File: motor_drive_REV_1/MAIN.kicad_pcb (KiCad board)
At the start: 2 copper layers, 71 parts, among them J1 Conn_01x02, J2 Conn_01x03, J3 Conn_01x06, J4 Conn_01x06, Q1 nmos, Q2 nmos, Q3 nmos, Q4 nmos, Q5 nmos, Q6 nmos, U1 AD8418ABRMZ-RL, U2 AD8418ABRMZ-RL, U3 AD8418ABRMZ-RL, U4 AD8418ABRMZ-RL, U5 ADA4571WHRZ-R7, U6 SN65LBC176QDRQ1, U7 FAN7888_gen, U8 TMS320F28027PTT, U9 AD8418ABRMZ-RL

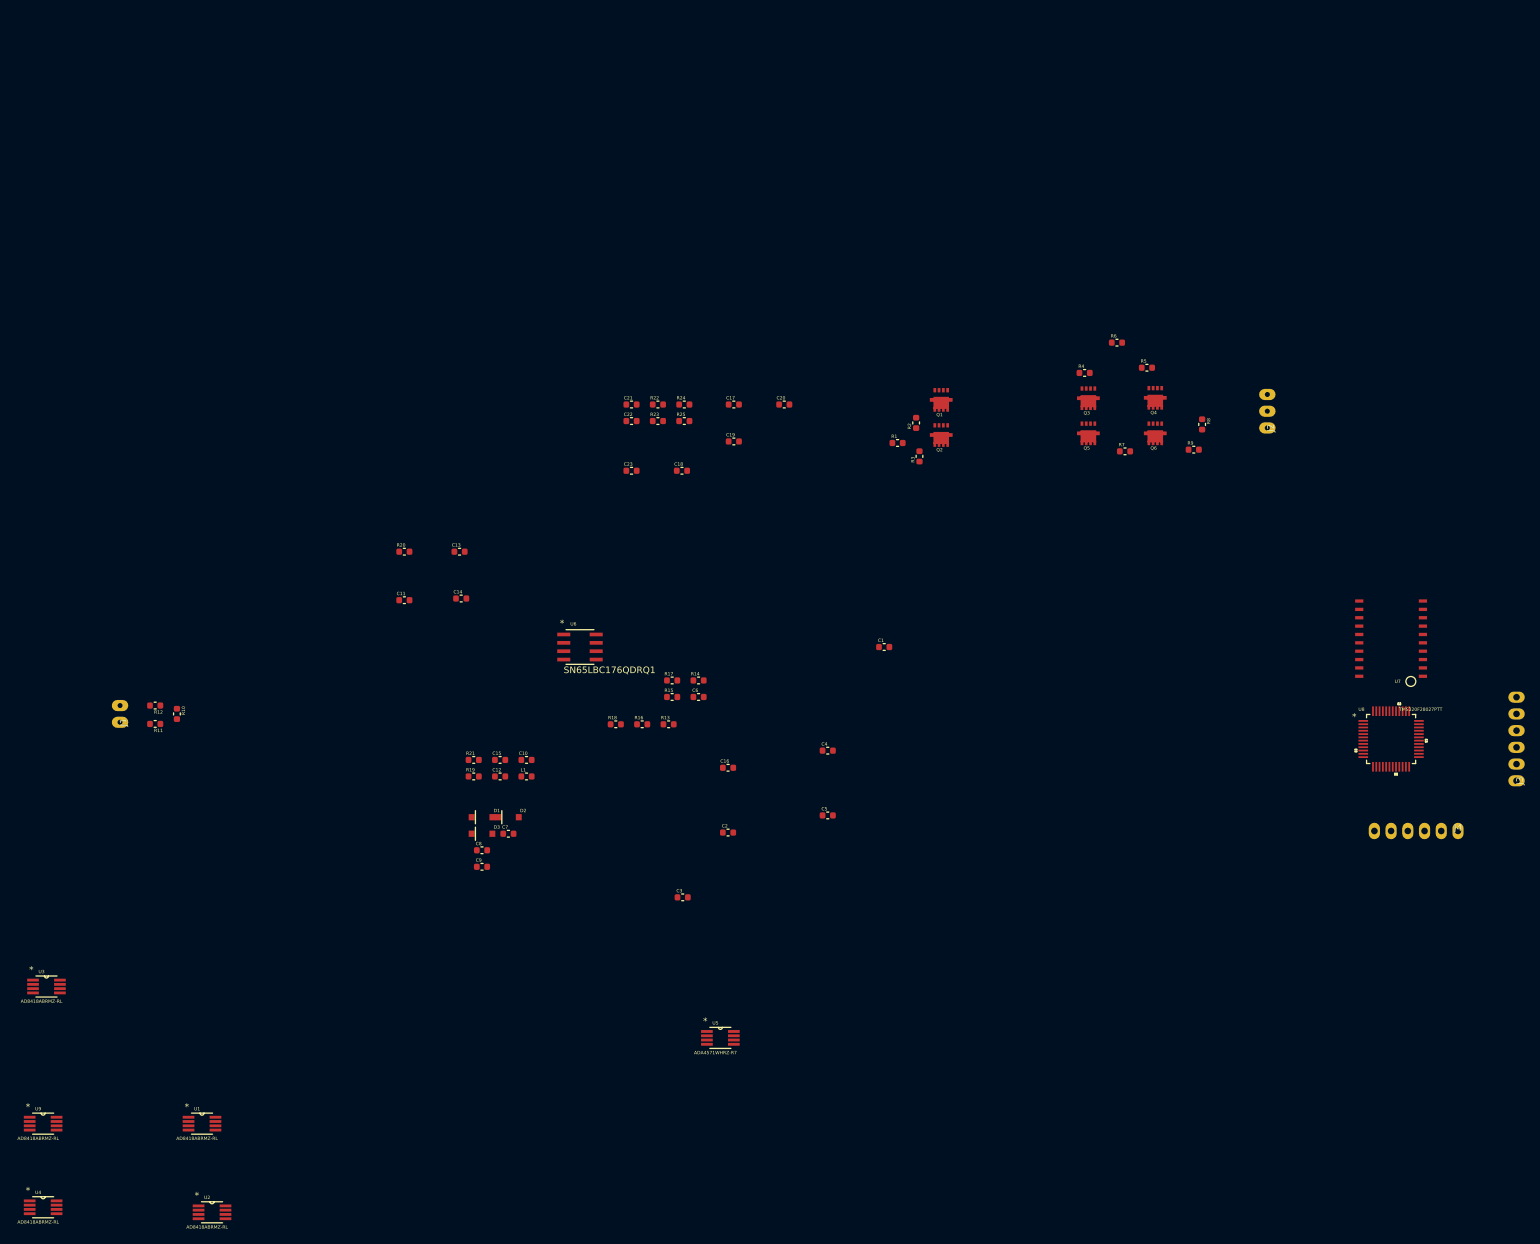
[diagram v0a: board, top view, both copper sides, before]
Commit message: working on adding thermistors but encountered too many hierarchicaly copies bug
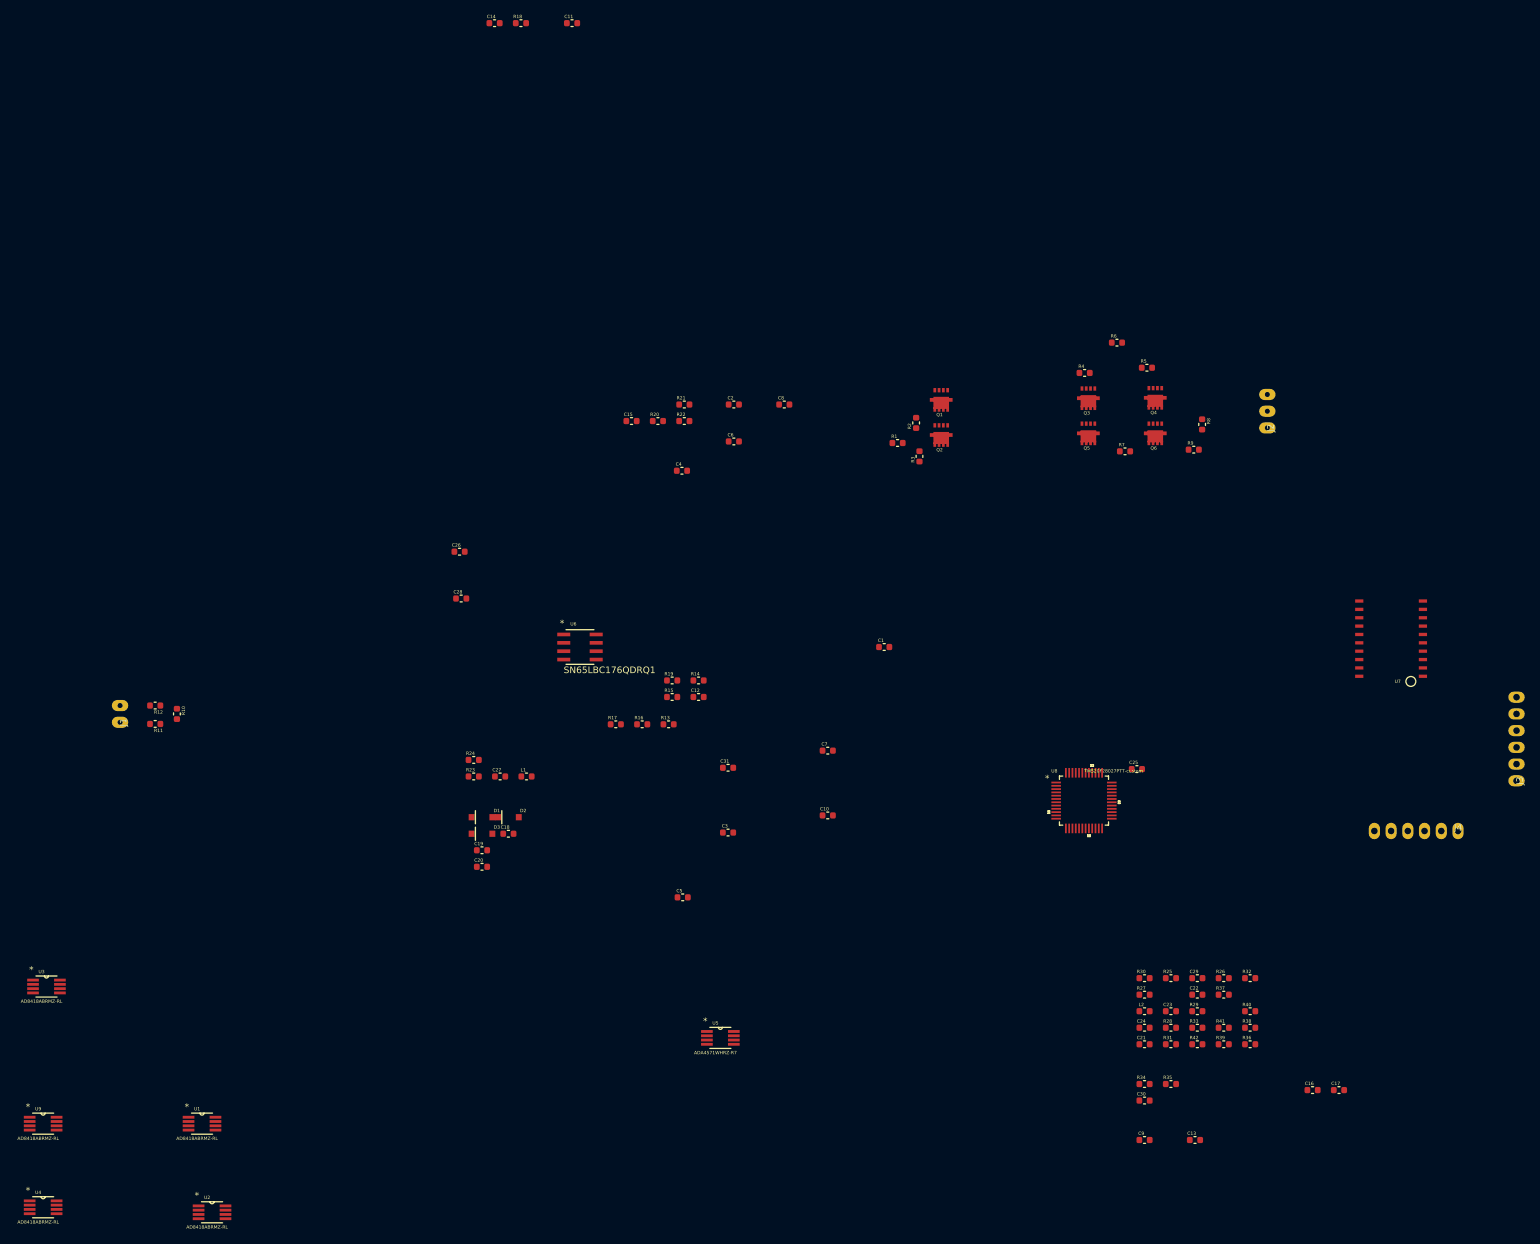
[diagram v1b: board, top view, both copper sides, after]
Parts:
- removed the C10 at (125.2, 97.2)
- removed the C15 at (121.2, 97.2)
- removed the R20 at (106.7, 65.5)
- removed the R22 at (145.2, 43.2)
- added C13: 0.01uF, motor_drive_footprints:C_0603_1608Metric, F.Cu at (226.8, 154.9)
- added C14: 680pF, motor_drive_footprints:C_0603_1608Metric, F.Cu at (120.4, -14.7)
- added C16: 2.2uF, motor_drive_footprints:C_0603_1608Metric, F.Cu at (244.6, 147.3)
- added C17: 0.01uF, motor_drive_footprints:C_0603_1608Metric, F.Cu at (248.6, 147.3)
- added C22: 2.2uF, motor_drive_footprints:C_0603_1608Metric, F.Cu at (227.1, 132.8)
- added C24: 0.01uF, motor_drive_footprints:C_0603_1608Metric, F.Cu at (219.1, 137.8)
- added C25: 4.7uF, motor_drive_footprints:C_0603_1608Metric, F.Cu at (217.9, 98.6)
- added C29: 1uF, motor_drive_footprints:C_0603_1608Metric, F.Cu at (227.1, 130.3)
- added C30: 1uF, motor_drive_footprints:C_0603_1608Metric, F.Cu at (219.1, 148.9)
- added C9: 0.01uF, motor_drive_footprints:C_0603_1608Metric, F.Cu at (219.1, 154.9)
- added L2: 2.2uF, motor_drive_footprints:C_0603_1608Metric, F.Cu at (219.1, 135.3)
- added R18: 680, motor_drive_footprints:C_0603_1608Metric, F.Cu at (124.4, -14.7)
- added R25: 375, motor_drive_footprints:C_0603_1608Metric, F.Cu at (223.1, 130.3)
- added R26: 2.2k, motor_drive_footprints:C_0603_1608Metric, F.Cu at (231.1, 130.3)
- added R27: 10k, motor_drive_footprints:C_0603_1608Metric, F.Cu at (219.1, 132.8)
- added R28: 10k, motor_drive_footprints:C_0603_1608Metric, F.Cu at (223.1, 137.8)
- added R29: 10k, motor_drive_footprints:C_0603_1608Metric, F.Cu at (227.1, 135.3)
- added R30: 10k, motor_drive_footprints:C_0603_1608Metric, F.Cu at (219.1, 130.3)
- added R31: 10k, motor_drive_footprints:C_0603_1608Metric, F.Cu at (223.1, 140.3)
- added R32: 10k, motor_drive_footprints:C_0603_1608Metric, F.Cu at (235.1, 130.3)
- added R33: 10k, motor_drive_footprints:C_0603_1608Metric, F.Cu at (227.1, 137.8)
- added R34: 10k, motor_drive_footprints:C_0603_1608Metric, F.Cu at (219.1, 146.4)
- added R35: 375, motor_drive_footprints:C_0603_1608Metric, F.Cu at (223.1, 146.4)
- added R36: 375, motor_drive_footprints:C_0603_1608Metric, F.Cu at (235.1, 140.3)
- added R37: 375, motor_drive_footprints:C_0603_1608Metric, F.Cu at (231.1, 132.8)
- added R38: 375, motor_drive_footprints:C_0603_1608Metric, F.Cu at (235.1, 137.8)
- added R39: 375, motor_drive_footprints:C_0603_1608Metric, F.Cu at (231.1, 140.3)
- added R40: 375, motor_drive_footprints:C_0603_1608Metric, F.Cu at (235.1, 135.3)
- added R41: 375, motor_drive_footprints:C_0603_1608Metric, F.Cu at (231.1, 137.8)
- added R42: 375, motor_drive_footprints:C_0603_1608Metric, F.Cu at (227.1, 140.3)
- C10: renamed from C5; value C -> 2.2uF
- C11: value C -> 0.01uF
- C12: renamed from C6; value C -> 2.2uF
- C15: renamed from C22; value C -> 680pF
- C18: renamed from C7; value C -> 0.22uF
- C19: renamed from C8; value C -> 0.22uF
- C20: renamed from C9; value C -> 0.22uF
- C21: value C -> 2.2uF
- C26: renamed from C13; value C -> 1uF
- C27: renamed from C12; value C -> 100pF
- C28: renamed from C14; value C -> 4.7uF
- C31: renamed from C16; value 1uF -> 0.01uF
- L1: value L -> 2.2uF
- R1, R2, R4, R5, R7, R8: value R -> 10
- R24: renamed from R21; value R -> 4.7k
- R3, R6, R9: value R -> 0.005
- U8: value TMS320F28027PTT -> TMS20F28027PTT-custom
- moved C21 124.5 mm to (219.1, 140.3)
- moved C23 116.0 mm to (223.1, 135.3)
- moved C11 91.3 mm to (132.1, -14.7)
- moved U8 47.6 mm to (209.9, 103.3)
- renumbered C17 to C2, C2 to C3, C18 to C4, C3 to C5, C19 to C6, C4 to C7, C20 to C8, R18 to R17, R17 to R19, R23 to R20, R24 to R21, R25 to R22, R19 to R23
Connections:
- C1 pad 1: /5.0V -> /GND
- C10 pad 2: /5.0V -> /GND
- C11 pad 1: /5.0V -> Net-(C11-Pad1)
- C11 pad 2: /5.0V -> Net-(C11-Pad2)
- C12 pad 2: /5.0V -> /GND
- C15 pad 1: /5.0V -> /GND
- C15 pad 2: /5.0V -> Net-(C15-Pad2)
- C2 pad 1: /5.0V -> /GND
- C21 pad 2: /5.0V -> /GND
- C23 pad 2: /5.0V -> /GND
- C26 pad 1: /5.0V -> Net-(C26-Pad1)
- C26 pad 2: /5.0V -> /GND
- C27 pad 1: /5.0V -> /GND
- C27 pad 2: Net-(C12-Pad2) -> /chip_reset
- C28 pad 1: Net-(C14-Pad1) -> Net-(C28-Pad1)
- C28 pad 2: /5.0V -> /GND
- C3 pad 1: /5.0V -> /GND
- C31 pad 1: /5.0V -> /GND
- C4 pad 1: /5.0V -> /GND
- C5 pad 1: /5.0V -> /GND
- C6 pad 1: /5.0V -> /GND
- C7 pad 1: /5.0V -> /GND
- C8 pad 1: /5.0V -> /GND
- J3 pad 3: /CLK -> /nEN
- J3 pad 4: /nEN -> /CLK
- J3 pad 6: /5.0V -> /GND
- J4 pad 6: /5.0V -> /GND
- L1 pad 1: Net-(C14-Pad1) -> Net-(C26-Pad1)
- R14 pad 2: /5.0V -> /GND
- R17 pad 1: /5.0V -> /GND
- R17 pad 2: /5.0V -> /balance
- R19 pad 1: /5.0V -> Net-(C14-Pad1)
- R19 pad 2: /5.0V -> Net-(C15-Pad2)
- R20 pad 1: /5.0V -> /GND
- R20 pad 2: /5.0V -> Net-(C15-Pad2)
- R21 pad 1: /5.0V -> Net-(C14-Pad1)
- R22 pad 1: /5.0V -> Net-(C15-Pad2)
- R23 pad 1: Net-(C12-Pad2) -> /GND
- R23 pad 2: /5.0V -> Net-(R23-Pad2)
- R24 pad 1: /5.0V -> /GND
- U1 pad 2: /5.0V -> /GND
- U1 pad 3: /5.0V -> /GND
- U2 pad 2: /5.0V -> /GND
- U2 pad 3: /5.0V -> /GND
- U3 pad 2: /5.0V -> /GND
- U3 pad 3: /5.0V -> /GND
- U4 pad 2: /5.0V -> /GND
- U4 pad 3: /5.0V -> /GND
- U5 pad 1: /5.0V -> /GND
- U5 pad 3: /5.0V -> /GND
- U5 pad 6: /5.0V -> /GND
- U5 pad 8: /5.0V -> /GND
- U6 pad 5: /5.0V -> /GND
- U6 pad 6: /5.0V -> Net-(C15-Pad2)
- U6 pad 7: /5.0V -> Net-(C14-Pad1)
- U7 pad 11: /5.0V -> /GND
- U8 pad 10: /I_sense_1 -> /cos
- U8 pad 11: Net-(C14-Pad1) -> Net-(C28-Pad1)
- U8 pad 12: /5.0V -> /GND
- U8 pad 15: /IDC_sense -> /therm_1
- U8 pad 16: /VDC_sense -> /therm_2
- U8 pad 2: /F28027/JTAG_nTRST -> Net-(R23-Pad2)
- U8 pad 20: /F28027/JTAG_TDI -> Net-(R28-Pad1)
- U8 pad 21: /F28027/JTAG_TMS -> Net-(R30-Pad1)
- U8 pad 22: /F28027/JTAG_TDO -> Net-(R32-Pad1)
- U8 pad 23: /F28027/JTAG_TCK -> Net-(R34-Pad1)
- U8 pad 24: /CLK -> Net-(R27-Pad1)
- U8 pad 25: /nEN -> Net-(R29-Pad1)
- U8 pad 26: /MISO -> Net-(R31-Pad1)
- U8 pad 27: /MOSI -> Net-(R33-Pad1)
- U8 pad 28: /LS_1 -> /HS_1
- U8 pad 29: /HS_1 -> /LS_1
- U8 pad 3: Net-(C12-Pad2) -> /chip_reset
- U8 pad 33: /5.0V -> /GND
- U8 pad 35: /5.0V -> Net-(C26-Pad1)
- U8 pad 4: /sin -> /I_sense_1
- U8 pad 43: /5.0V -> /GND
- U8 pad 45: /5.0V -> Net-(U8-Pad45)
- U8 pad 5: /VDC_sense -> /I_sense_2
- U8 pad 6: /cos -> /I_sense_3
- U8 pad 8: /I_sense_2 -> /VDC_sense
- U8 pad 9: /I_sense_3 -> /sin
- U9 pad 2: /5.0V -> /GND
- U9 pad 3: /5.0V -> /GND

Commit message: started layout
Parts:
- removed the J2 at (237.7, 46.7)
- added C11: 1uF, motor_drive_footprints:gen_0805, F.Cu at (232.2, 150.9)
- added C12: 1uF, motor_drive_footprints:gen_0805, F.Cu at (227.9, 150.9)
- added C34: 0.01uF, motor_drive_footprints:C_0603_1608Metric, F.Cu at (158.0, 111.0)
- added C35: 0.01uF, motor_drive_footprints:C_0603_1608Metric, F.Cu at (147.3, 103.4)
- added C36: 4.7uF, motor_drive_footprints:C_0603_1608Metric, F.Cu at (158.0, 107.4)
- added C37: 1uF, motor_drive_footprints:C_0603_1608Metric, F.Cu at (158.0, 109.2)
- added C38: 100pF, motor_drive_footprints:C_0603_1608Metric, F.Cu at (140.4, 109.0)
- added C39: 4.7uF, motor_drive_footprints:C_0603_1608Metric, F.Cu at (140.5, 112.5)
- added C40: 1uF, motor_drive_footprints:C_0603_1608Metric, F.Cu at (140.5, 116.1)
- added C41: 1uF, motor_drive_footprints:C_0603_1608Metric, F.Cu at (74.8, 113.3)
- added C42: 0.01uF, motor_drive_footprints:C_0603_1608Metric, F.Cu at (78.8, 113.3)
- added C43: C, motor_drive_footprints:C_0603_1608Metric, F.Cu at (140.2, 95.2)
- added C44: C, motor_drive_footprints:C_0603_1608Metric, F.Cu at (147.8, 97.3)
- added J1: Conn_01x04, motor_drive_footprints:4pos_254, F.Cu at (122.9, 89.9)
- added J3: Conn_01x04, motor_drive_footprints:4pos_338, F.Cu at (249.4, 109.5)
- added J6: Conn_01x02, motor_drive_footprints:2pos_254, F.Cu at (139.5, 92.2)
- added J7: Conn_01x02, motor_drive_footprints:2pos_254, F.Cu at (147.2, 92.2)
- added R43: R, motor_drive_footprints:C_0603_1608Metric, F.Cu at (140.2, 97.3)
- added R44: R, motor_drive_footprints:C_0603_1608Metric, F.Cu at (147.8, 95.2)
- C10: value 2.2uF -> 1uF; footprint motor_drive_footprints:C_0603_1608Metric -> motor_drive_footprints:gen_0805
- C13: renamed from C11; value 0.01uF -> 1uF; footprint motor_drive_footprints:C_0603_1608Metric -> motor_drive_footprints:gen_0805
- C14: renamed from C12; value 2.2uF -> 1uF; footprint motor_drive_footprints:C_0603_1608Metric -> motor_drive_footprints:gen_0805
- C15: renamed from C13; value 0.01uF -> 1uF; footprint motor_drive_footprints:C_0603_1608Metric -> motor_drive_footprints:gen_0805
- C16: renamed from C14; value 680pF -> 1uF; footprint motor_drive_footprints:C_0603_1608Metric -> motor_drive_footprints:gen_0805
- C17: renamed from C15; value 680pF -> 1uF; footprint motor_drive_footprints:C_0603_1608Metric -> motor_drive_footprints:gen_0805
- C18: renamed from C16; value 2.2uF -> 1uF; footprint motor_drive_footprints:C_0603_1608Metric -> motor_drive_footprints:gen_0805
- C19: renamed from C17; value 0.01uF -> 1uF; footprint motor_drive_footprints:C_0603_1608Metric -> motor_drive_footprints:gen_0805
- C20: renamed from C18; value 0.22uF -> 1uF; footprint motor_drive_footprints:C_0603_1608Metric -> motor_drive_footprints:gen_0805
- C21: renamed from C19; value 0.22uF -> 2.2uF
- C22: renamed from C20; value 0.22uF -> 0.01uF
- C24: renamed from C22; value 2.2uF -> 0.01uF
- C25: renamed from C23; value 0.01uF -> 680pF
- C26: renamed from C24; value 0.01uF -> 680pF
- C27: renamed from C25; value 4.7uF -> 2.2uF
- C28: renamed from C26; value 1uF -> 0.01uF
- C29: renamed from C27; value 100pF -> 0.22uF
- C30: renamed from C28; value 4.7uF -> 0.22uF
- C31: renamed from C29; value 1uF -> 0.22uF
- C32: renamed from C30; value 1uF -> 2.2uF
- C33: renamed from C31; value 0.01uF -> 2.2uF
- C9: value 0.01uF -> 1uF; footprint motor_drive_footprints:C_0603_1608Metric -> motor_drive_footprints:gen_0805
- R3, R6, R9: value 0.005 -> WSL20101L000FEA18; footprint motor_drive_footprints:C_0603_1608Metric -> motor_drive_footprints:WSL20101L000FEA18
- moved C19 197.5 mm to (66.8, 70.3)
- moved C18 192.3 mm to (66.8, 74.2)
- moved C15 182.7 mm to (66.8, 66.5)
- moved C9 178.0 mm to (66.8, 62.7)
- moved C8 141.7 mm to (75.7, 153.7)
- moved C24 125.9 mm to (111.5, 83.1), turned to 180 degrees
- moved C6 125.6 mm to (75.7, 144.8)
- moved C23 122.6 mm to (111.5, 81.5), turned to 180 degrees
- moved C25 118.3 mm to (117.9, 81.3)
- moved J5 114.5 mm to (153.7, 126.5)
- moved C26 113.1 mm to (117.9, 87.4), turned to 180 degrees
- moved C2 112.7 mm to (74.9, 120.7)
- moved C1 111.3 mm to (74.9, 118.1)
- moved C30 111.1 mm to (213.4, 124.9), turned to 270 degrees
- moved C7 109.5 mm to (75.7, 149.6)
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- renumbered C21 to C23, J1 to J2, J3 to J4, J4 to J5, R12 to R10, R10 to R11, R11 to R12
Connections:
- C10 pad 1: /5.0V -> /DC_Link_Input/5.0V
- C10 pad 2: /GND -> /DC_Link_Input/GND
- C13 pad 1: Net-(C11-Pad1) -> /DC_Link_Input/5.0V
- C13 pad 2: Net-(C11-Pad2) -> /DC_Link_Input/GND
- C14 pad 1: /5.0V -> /DC_Link_Input/5.0V
- C14 pad 2: /GND -> /DC_Link_Input/GND
- C15 pad 1: /5.0V -> /DC_Link_Input/5.0V
- C15 pad 2: /GND -> /DC_Link_Input/GND
- C16 pad 1: Net-(C14-Pad1) -> /DC_Link_Input/5.0V
- C16 pad 2: /5.0V -> /DC_Link_Input/GND
- C17 pad 1: /GND -> /DC_Link_Input/5.0V
- C17 pad 2: Net-(C15-Pad2) -> /DC_Link_Input/GND
- C18 pad 1: /5.0V -> /DC_Link_Input/5.0V
- C18 pad 2: /GND -> /DC_Link_Input/GND
- C19 pad 1: /5.0V -> /DC_Link_Input/5.0V
- C19 pad 2: /GND -> /DC_Link_Input/GND
- C20 pad 1: Net-(C18-Pad1) -> /DC_Link_Input/5.0V
- C20 pad 2: /I_sense_p1 -> /DC_Link_Input/GND
- C21 pad 1: Net-(C19-Pad1) -> /5.0V
- C21 pad 2: /I_sense_p2 -> /GND
- C22 pad 1: Net-(C20-Pad1) -> (no net)
- C22 pad 2: /I_sense_p3 -> (no net)
- C25 pad 1: /5.0V -> Net-(C25-Pad1)
- C25 pad 2: /GND -> /5.0V
- C26 pad 1: /5.0V -> /GND
- C26 pad 2: /GND -> Net-(C26-Pad2)
- C28 pad 1: Net-(C26-Pad1) -> /5.0V
- C29 pad 1: /GND -> Net-(C29-Pad1)
- C29 pad 2: /chip_reset -> /I_sense_p1
- C30 pad 1: Net-(C28-Pad1) -> Net-(C30-Pad1)
- C30 pad 2: /GND -> /I_sense_p2
- C31 pad 1: /5.0V -> Net-(C31-Pad1)
- C31 pad 2: /GND -> /I_sense_p3
- C32 pad 1: /GND -> /5.0V
- C32 pad 2: /5.0V -> /GND
- C33 pad 1: /GND -> /5.0V
- C33 pad 2: /5.0V -> /GND
- D1 pad 1: Net-(C18-Pad1) -> Net-(C29-Pad1)
- D2 pad 1: Net-(C19-Pad1) -> Net-(C30-Pad1)
- D3 pad 1: Net-(C20-Pad1) -> Net-(C31-Pad1)
- J2 pad 2: /IDC_sense_n -> /IDC_sense_p
- L1 pad 1: Net-(C26-Pad1) -> Net-(C37-Pad1)
- L2 pad 2: Net-(C28-Pad1) -> Net-(C39-Pad1)
- R10 pad 2: /IDC_sense_n -> /IDC_sense_p
- R18 pad 1: Net-(C14-Pad1) -> Net-(C25-Pad1)
- R19 pad 1: Net-(C14-Pad1) -> Net-(C25-Pad1)
- R19 pad 2: Net-(C15-Pad2) -> Net-(C26-Pad2)
- R20 pad 2: Net-(C15-Pad2) -> Net-(C26-Pad2)
- R21 pad 1: Net-(C14-Pad1) -> Net-(C25-Pad1)
- R22 pad 1: Net-(C15-Pad2) -> Net-(C26-Pad2)
- U1 pad 1: /I_sense_2n -> (no net)
- U1 pad 4: Net-(U1-Pad4) -> (no net)
- U1 pad 8: /I_sense_2p -> (no net)
- U2 pad 1: /I_sense_3n -> (no net)
- U2 pad 4: Net-(U2-Pad4) -> (no net)
- U2 pad 8: /I_sense_3p -> (no net)
- U3 pad 1: /IDC_sense_n -> /DC_pos
- U3 pad 4: Net-(U3-Pad4) -> (no net)
- U3 pad 8: /DC_pos -> /IDC_sense_p
- U4 pad 4: Net-(U4-Pad4) -> (no net)
- U5 pad 5: Net-(U5-Pad5) -> (no net)
- U6 pad 6: Net-(C15-Pad2) -> Net-(C26-Pad2)
- U6 pad 7: Net-(C14-Pad1) -> Net-(C25-Pad1)
- U7 pad 10: Net-(C20-Pad1) -> Net-(C31-Pad1)
- U7 pad 16: Net-(C19-Pad1) -> Net-(C30-Pad1)
- U7 pad 20: Net-(C18-Pad1) -> Net-(C29-Pad1)
- U8 pad 11: Net-(C28-Pad1) -> Net-(C39-Pad1)
- U8 pad 19: /LED_0 -> (no net)
- U8 pad 30: Net-(U8-Pad30) -> (no net)
- U8 pad 31: /LED_2 -> (no net)
- U8 pad 35: Net-(C26-Pad1) -> Net-(C37-Pad1)
- U8 pad 36: /LED_1 -> (no net)
- U8 pad 41: /BUTTON_1 -> (no net)
- U8 pad 42: /BUTTON_0 -> (no net)
- U8 pad 45: Net-(U8-Pad45) -> (no net)
- U8 pad 46: Net-(U8-Pad46) -> (no net)
- U9 pad 1: /I_sense_1n -> (no net)
- U9 pad 4: Net-(U9-Pad4) -> (no net)
- U9 pad 8: /I_sense_1p -> (no net)
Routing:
- net /GND: track 0.00 -> 27.6 mm, vias 0 -> 3
- net /5.0V: track 0.00 -> 18.8 mm, vias 0 -> 3
- net Net-(C25-Pad1): track 0.00 -> 9.58 mm
- net Net-(C26-Pad2): track 0.00 -> 9.39 mm
- net /DEnRE: track 0.00 -> 7.47 mm
- net /A: track 0.00 -> 5.77 mm
- net /balance: track 0.00 -> 5.53 mm
- net /B: track 0.00 -> 5.16 mm, vias 0 -> 1
- net Net-(R16-Pad2): track 0.00 -> 4.76 mm
- net Net-(R15-Pad2): track 0.00 -> 4.66 mm

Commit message: layout
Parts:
- moved C22 14.4 mm to (118.2, 122.2)
- moved C42 14.4 mm to (68.1, 103.6)
- moved C21 13.9 mm to (118.2, 120.5)
- moved C41 13.0 mm to (68.0, 102.1)
- moved U5 12.6 mm to (118.4, 117.1), turned to 180 degrees
- moved R24 10.4 mm to (158.2, 114.3)
- moved J7 8.14 mm to (155.3, 91.7)
- moved C44 8.14 mm to (156.0, 96.8)
- moved R44 8.14 mm to (155.9, 94.7)
- moved C2 8.03 mm to (68.3, 116.1)
- moved C6 8.01 mm to (69.1, 140.2)
- moved C1 7.50 mm to (68.3, 114.6)
- moved C5 7.50 mm to (69.1, 138.7)
- moved C8 6.84 mm to (69.3, 151.1)
- moved U9 6.61 mm to (68.1, 106.9)
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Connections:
- C22 pad 1: (no net) -> /5.0V
- C22 pad 2: (no net) -> /GND
- J4 pad 1: /MISO -> /MOSI
- J4 pad 2: /MOSI -> /MISO
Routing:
- net /GND: track 27.6 -> 79.9 mm
- net /5.0V: track 18.8 -> 67.0 mm, vias 3 -> 7
- net Net-(R33-Pad1): track 0.00 -> 24.5 mm
- net Net-(R31-Pad1): track 0.00 -> 18.4 mm
- net Net-(R29-Pad1): track 0.00 -> 14.5 mm
- net Net-(R28-Pad1): track 0.00 -> 13.7 mm
- net Net-(R27-Pad1): track 0.00 -> 12.3 mm
- net Net-(R30-Pad1): track 0.00 -> 10.2 mm
- net Net-(R32-Pad1): track 0.00 -> 8.66 mm
- net Net-(R34-Pad1): track 0.00 -> 8.50 mm
- net Net-(C39-Pad1): track 0.00 -> 6.36 mm
- net /F28027/JTAG_TDI: track 0.00 -> 6.23 mm
- net Net-(R23-Pad2): track 0.00 -> 6.11 mm
- net Net-(C37-Pad1): track 0.00 -> 5.86 mm
- net /chip_reset: track 0.00 -> 5.74 mm
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
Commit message: layout
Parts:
- moved C5 111.7 mm to (162.6, 77.5)
- moved C6 111.7 mm to (162.6, 79.0)
- moved U3 111.7 mm to (162.6, 82.3)
- moved C7 110.6 mm to (153.7, 78.0)
- moved C8 110.6 mm to (153.7, 79.5)
- moved U4 110.6 mm to (153.7, 82.8)
- moved C1 100.4 mm to (168.7, 116.8)
- moved C2 100.4 mm to (168.7, 118.4)
- moved U1 100.4 mm to (168.7, 121.7)
- moved J2 98.4 mm to (158.8, 66.5), turned to 0 degrees
- moved R10 94.8 mm to (161.5, 71.3), turned to 90 degrees
- moved R11 93.2 mm to (159.5, 71.4), turned to 90 degrees
- moved R12 93.1 mm to (157.0, 69.8), turned to 90 degrees
- moved U9 90.8 mm to (157.7, 121.4)
- moved C41 90.8 mm to (157.7, 116.6)
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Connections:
- U1 pad 1: (no net) -> /I_sense_n2
- U1 pad 8: (no net) -> /I_sense_p2
- U2 pad 1: (no net) -> /I_sense_n3
- U2 pad 8: (no net) -> /I_sense_p3
- U9 pad 1: (no net) -> /I_sense_n1
- U9 pad 8: (no net) -> /I_sense_p1
